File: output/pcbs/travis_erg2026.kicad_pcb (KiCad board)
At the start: 2 copper layers, 167.2 x 170.9 mm, 182 parts

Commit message: bunch of documentation
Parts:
- C10, C11, C12, C13, C14, C15, C16, C17, C18, C19, C2, C20, C21, C22, C23, C24, C25, C26, C27, C28, C29, C3, C30, C31, C32, C33, C34, C35, C36, C37, C38, C39, C4, C40, C41, C5, C6, C7, C8, C9: value C_1206_3216Metric -> C710467
- LED1, LED10, LED11, LED12, LED13, LED14, LED15, LED16, LED17, LED18, LED19, LED2, LED20, LED21, LED22, LED23, LED24, LED25, LED26, LED27, LED28, LED29, LED3, LED30, LED31, LED32, LED33, LED34, LED35, LED36, LED37, LED38, LED39, LED4, LED40, LED5, LED6, LED7, LED8, LED9: value SK6812mini-e -> C5378731
- S1, S10, S11, S12, S13, S14, S15, S16, S17, S18, S19, S2, S20, S21, S22, S23, S24, S25, S26, S27, S28, S29, S3, S30, S31, S32, S33, S34, S35, S36, S37, S38, S39, S4, S40, S5, S6, S7, S8, S9: value Kailh MX Switch Sockets -> C41430893

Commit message: BOM and CPL progress
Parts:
- LED1, LED10, LED11, LED12, LED13, LED14, LED15, LED16, LED17, LED18, LED19, LED2, LED20, LED21, LED22, LED23, LED24, LED25, LED26, LED27, LED28, LED29, LED3, LED30, LED31, LED32, LED33, LED34, LED35, LED36, LED37, LED38, LED39, LED4, LED40, LED5, LED6, LED7, LED8, LED9: footprint travis:led_SK6812mini-e (per-key, single-side) -> led_SK6812mini-e (per-key, single-side)
- S1, S10, S11, S12, S13, S14, S15, S16, S17, S18, S19, S2, S20, S21, S22, S23, S24, S25, S26, S27, S28, S29, S3, S30, S31, S32, S33, S34, S35, S36, S37, S38, S39, S4, S40, S5, S6, S7, S8, S9: footprint travis:MX -> MX

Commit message: attempt 2
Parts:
- removed LED1, LED2, LED3, LED4, LED5, LED6, LED7, LED8, LED9: C5378731, led_SK6812mini-e (per-key, single-side)
- added LED01: C5378731, led_SK6812mini-e (per-key, single-side), B.Cu at (176.2, 89.1)
- added LED02: C5378731, led_SK6812mini-e (per-key, single-side), B.Cu at (153.9, 87.1)
- added LED03: C5378731, led_SK6812mini-e (per-key, single-side), B.Cu at (132.0, 85.7)
- added LED04: C5378731, led_SK6812mini-e (per-key, single-side), B.Cu at (110.0, 84.7)
- added LED05: C5378731, led_SK6812mini-e (per-key, single-side), B.Cu at (88.0, 86.1)
- added LED06: C5378731, led_SK6812mini-e (per-key, single-side), B.Cu at (66.1, 87.8)
- added LED07: C5378731, led_SK6812mini-e (per-key, single-side), B.Cu at (43.9, 90.1)
- added LED08: C5378731, led_SK6812mini-e (per-key, single-side), B.Cu at (45.0, 111.2)
- added LED09: C5378731, led_SK6812mini-e (per-key, single-side), B.Cu at (66.9, 108.8)
- D1, D10, D11, D12, D13, D14, D15, D16, D17, D18, D19, D2, D20, D21, D22, D23, D24, D25, D26, D27, D28, D29, D3, D30, D31, D32, D33, D34, D35, D36, D37, D38, D39, D4, D40, D5, D6, D7, D8, D9: value D_1206_3216Metric -> C7420318
- MCU1: value RP2040 Pro Micro -> RP2040 Community Edition
- S1, S10, S11, S12, S13, S14, S15, S16, S17, S18, S19, S2, S20, S21, S22, S23, S24, S25, S26, S27, S28, S29, S3, S30, S31, S32, S33, S34, S35, S36, S37, S38, S39, S4, S40, S5, S6, S7, S8, S9: footprint MX -> ceoloide:switch_mx; moved to B.Cu
- moved LED21 137.1 mm to (46.1, 132.2), turned to 183 degrees
- moved LED35 107.2 mm to (48.3, 174.2), turned to 183 degrees
- moved LED20 106.4 mm to (67.6, 129.9), turned to 182 degrees
- moved LED29 106.4 mm to (171.8, 173.2), turned to 177 degrees
- moved LED37 104.5 mm to (89.9, 191.3), turned to 1 degrees
- moved LED36 102.2 mm to (59.7, 194.5), turned to 4 degrees
- moved LED19 94.4 mm to (88.8, 128.2), turned to 181 degrees
- moved LED40 84.7 mm to (160.4, 193.5), turned to -4 degrees
- moved LED28 83.8 mm to (172.9, 152.2), turned to -3 degrees
- moved LED26 75.5 mm to (130.9, 148.9), turned to -1 degrees
- moved LED27 74.2 mm to (151.7, 150.2), turned to -2 degrees
- moved LED34 66.0 mm to (69.1, 172.0), turned to 182 degrees
- moved LED13 65.8 mm to (153.2, 108.1), turned to -2 degrees
- moved LED10 65.4 mm to (88.4, 107.1), turned to 1 degrees
- moved LED32 63.2 mm to (110.0, 168.9), turned to 180 degrees
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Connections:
- LED10 pad 2: LED_33 -> LED11
- LED10 pad 4: LED_32 -> LED10
- LED11 pad 2: LED_19 -> LED12
- LED11 pad 4: LED_18 -> LED11
- LED12 pad 2: LED_5 -> LED13
- LED12 pad 4: LED_4 -> LED12
- LED13 pad 2: LED_32 -> LED14
- LED13 pad 4: LED_31 -> LED13
- LED14 pad 2: LED_18 -> LED15
- LED14 pad 4: LED_17 -> LED14
- LED15 pad 2: LED_4 -> LED16
- LED15 pad 4: LED_3 -> LED15
- LED16 pad 2: LED_31 -> LED17
- LED16 pad 4: LED_30 -> LED16
- LED17 pad 2: LED_17 -> LED18
- LED17 pad 4: LED_16 -> LED17
- LED18 pad 2: LED_3 -> LED19
- LED18 pad 4: LED_2 -> LED18
- LED19 pad 2: LED_30 -> LED20
- LED19 pad 4: LED_29 -> LED19
- LED20 pad 2: LED_16 -> LED21
- LED20 pad 4: LED_15 -> LED20
- LED21 pad 2: LED_2 -> LED22
- LED21 pad 4: LED_1 -> LED21
- LED22 pad 2: LED_37 -> LED23
- LED22 pad 4: LED_36 -> LED22
- LED23 pad 2: LED_23 -> LED24
- LED23 pad 4: LED_22 -> LED23
- LED24 pad 2: LED_9 -> LED25
- LED24 pad 4: LED_8 -> LED24
- LED25 pad 2: LED_24 -> LED26
- LED25 pad 4: LED_23 -> LED25
- LED26 pad 2: LED_10 -> LED27
- LED26 pad 4: LED_9 -> LED26
- LED27 pad 2: LED_38 -> LED28
- LED27 pad 4: LED_37 -> LED27
- LED28 pad 2: LED_25 -> LED29
- LED28 pad 4: LED_24 -> LED28
- LED29 pad 2: LED_11 -> LED30
- LED29 pad 4: LED_10 -> LED29
- LED30 pad 2: LED_39 -> LED31
- LED30 pad 4: LED_38 -> LED30
- LED31 pad 2: LED_26 -> LED32
- LED31 pad 4: LED_25 -> LED31
- LED32 pad 2: LED_12 -> LED33
- LED32 pad 4: LED_11 -> LED32
- LED33 pad 2: LED_40 -> LED34
- LED33 pad 4: LED_39 -> LED33
- LED34 pad 2: LED_27 -> LED35
- LED34 pad 4: LED_26 -> LED34
- LED35 pad 2: LED_13 -> LED36
- LED35 pad 4: LED_12 -> LED35
- LED36 pad 2: LED_28 -> LED37
- LED36 pad 4: LED_27 -> LED36
- LED37 pad 2: LED_14 -> LED38
- LED37 pad 4: LED_13 -> LED37
- LED38 pad 2: (no net) -> LED39
- LED38 pad 4: LED_40 -> LED38
- LED39 pad 2: LED_29 -> LED40
- LED39 pad 4: LED_28 -> LED39
- LED40 pad 2: LED_15 -> (no net)
- LED40 pad 4: LED_14 -> LED40
- MCU1 pad 31: LED_1 -> LED01
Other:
- board text added: "LED01"
- board text added: "LED02"
- board text added: "LED03"
- board text added: "LED04"
- board text added: "LED05"
- board text added: "LED06"
- board text added: "LED07"
- board text added: "LED08"
- board text added: "LED09"
- board text added: "LED10"
- board text added: "LED11"
- board text added: "LED12"
- board text added: "LED13"
- board text added: "LED14"
- board text added: "LED15"
- board text added: "LED16"
- board text added: "LED17"
- board text added: "LED18"
- board text added: "LED19"
- board text added: "LED20"
- board text added: "LED21"
- board text added: "LED22"
- board text added: "LED23"
- board text added: "LED24"
- board text added: "LED25"
- board text added: "LED26"
- board text added: "LED27"
- board text added: "LED28"
- board text added: "LED29"
- board text added: "LED30"
- board text added: "LED31"
- board text added: "LED32"
- board text added: "LED33"
- board text added: "LED34"
- board text added: "LED35"
- board text added: "LED36"
- board text added: "LED37"
- board text added: "LED38"
- board text added: "LED39"
- board text added: "LED40"
- board text removed: "LED_1"
- board text removed: "LED_10"
- board text removed: "LED_11"
- board text removed: "LED_12"
- board text removed: "LED_13"
- board text removed: "LED_14"
- board text removed: "LED_15"
- board text removed: "LED_16"
- board text removed: "LED_17"
- board text removed: "LED_18"
- board text removed: "LED_19"
- board text removed: "LED_2"
- board text removed: "LED_20"
- board text removed: "LED_21"
- board text removed: "LED_22"
- board text removed: "LED_23"
- board text removed: "LED_24"
- board text removed: "LED_25"
- board text removed: "LED_26"
- board text removed: "LED_27"
- board text removed: "LED_28"
- board text removed: "LED_29"
- board text removed: "LED_3"
- board text removed: "LED_30"
- board text removed: "LED_31"
- board text removed: "LED_32"
- board text removed: "LED_33"
- board text removed: "LED_34"
- board text removed: "LED_35"
- board text removed: "LED_36"
- board text removed: "LED_37"
- board text removed: "LED_38"
- board text removed: "LED_39"
- board text removed: "LED_4"
- board text removed: "LED_40"
- board text removed: "LED_5"
- board text removed: "LED_6"
- board text removed: "LED_7"
- board text removed: "LED_8"
- board text removed: "LED_9"
- board text removed: "S1"
- board text removed: "S10"
- board text removed: "S11"
- board text removed: "S12"
- board text removed: "S13"
- board text removed: "S14"
- board text removed: "S15"
- board text removed: "S16"
- board text removed: "S17"
- board text removed: "S18"
- board text removed: "S19"
- board text removed: "S2"
- board text removed: "S20"
- board text removed: "S21"
- board text removed: "S22"
- board text removed: "S23"
- board text removed: "S24"
- board text removed: "S25"
- board text removed: "S26"
- board text removed: "S27"
- board text removed: "S28"
- board text removed: "S29"
- board text removed: "S3"
- board text removed: "S30"
- board text removed: "S31"
- board text removed: "S32"
- board text removed: "S33"
- board text removed: "S34"
- board text removed: "S35"
- board text removed: "S36"
- board text removed: "S37"
- board text removed: "S38"
- board text removed: "S39"
- board text removed: "S4"
- board text removed: "S40"
- board text removed: "S5"
- board text removed: "S6"
- board text removed: "S7"
- board text removed: "S8"
- board text removed: "S9"

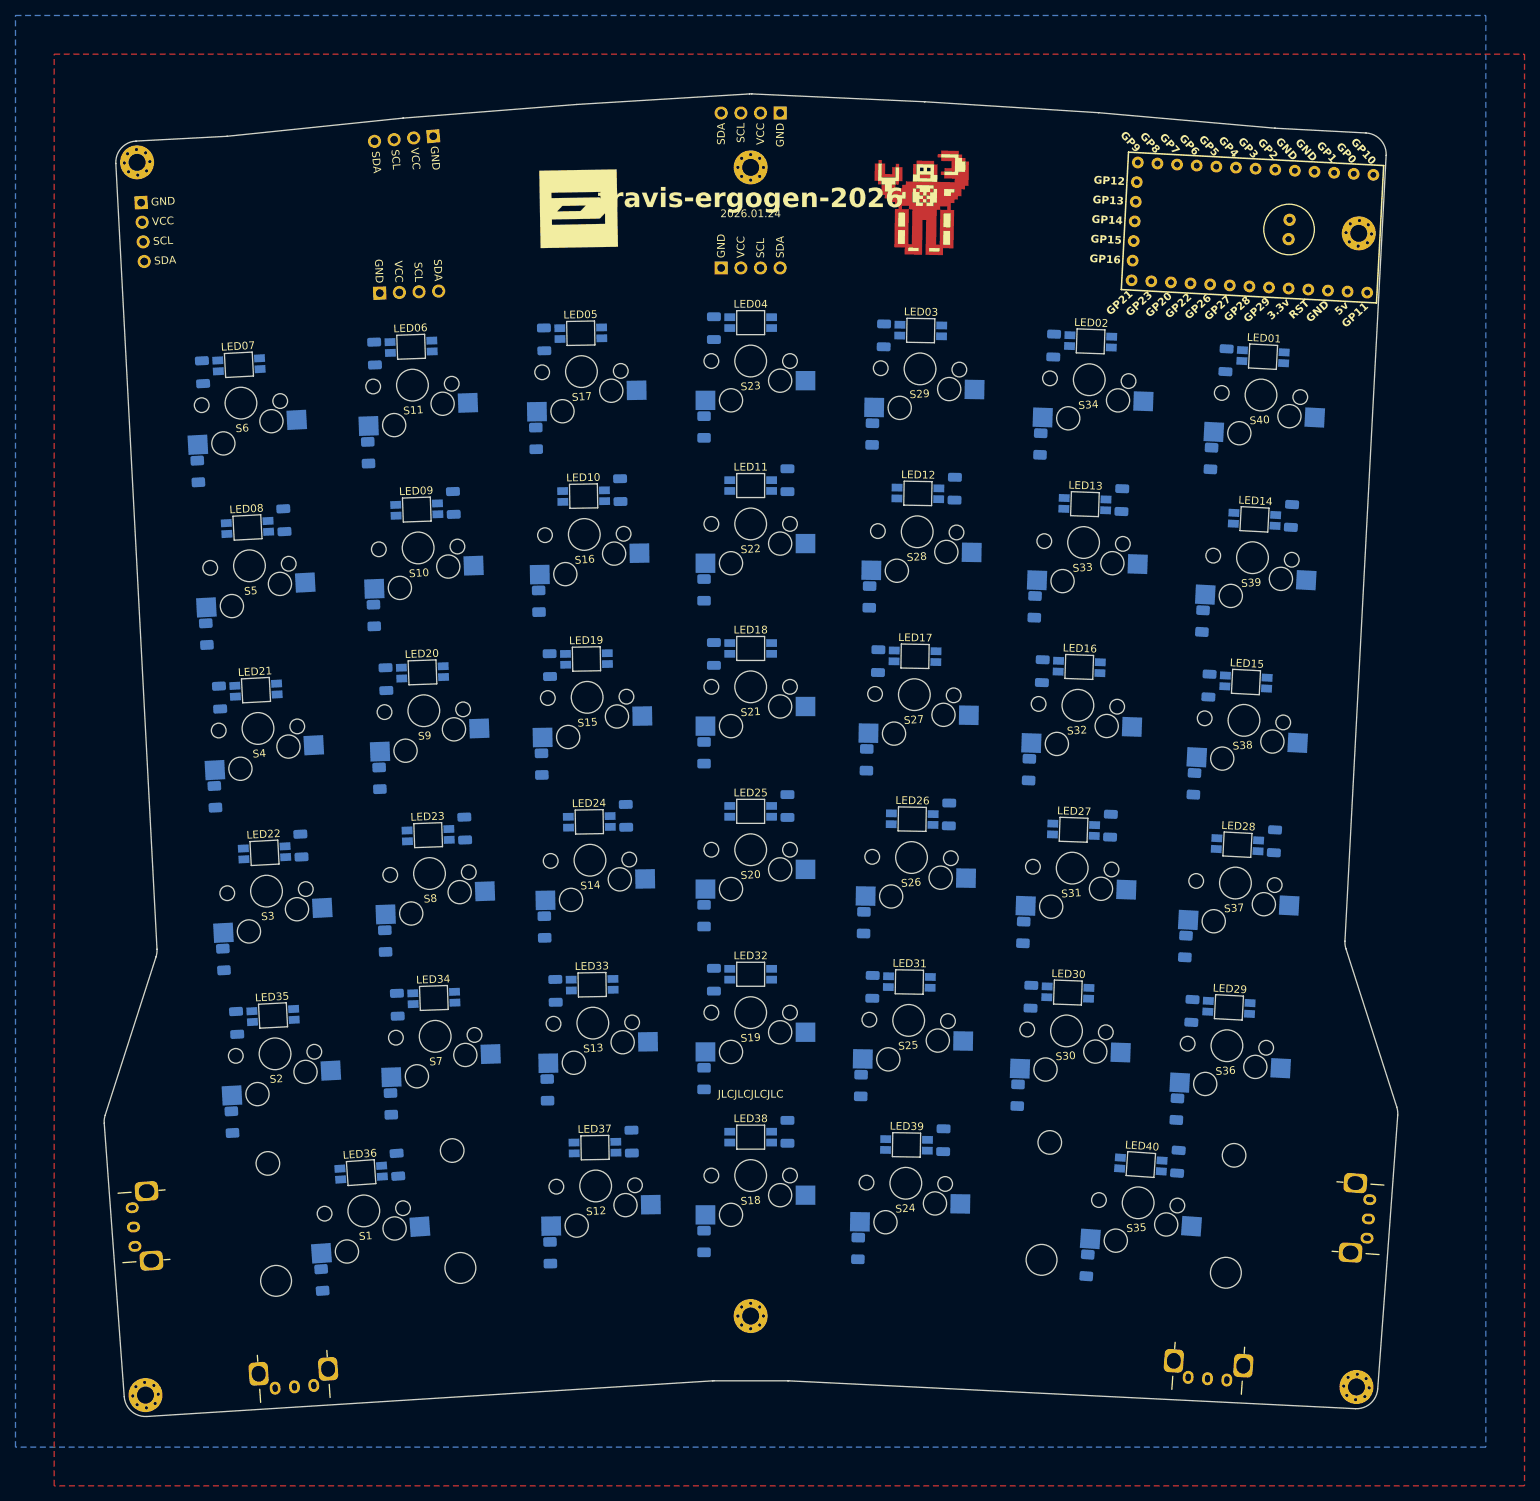
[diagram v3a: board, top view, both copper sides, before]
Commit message: fix encorder, organize datasheets, add easy routes and vias
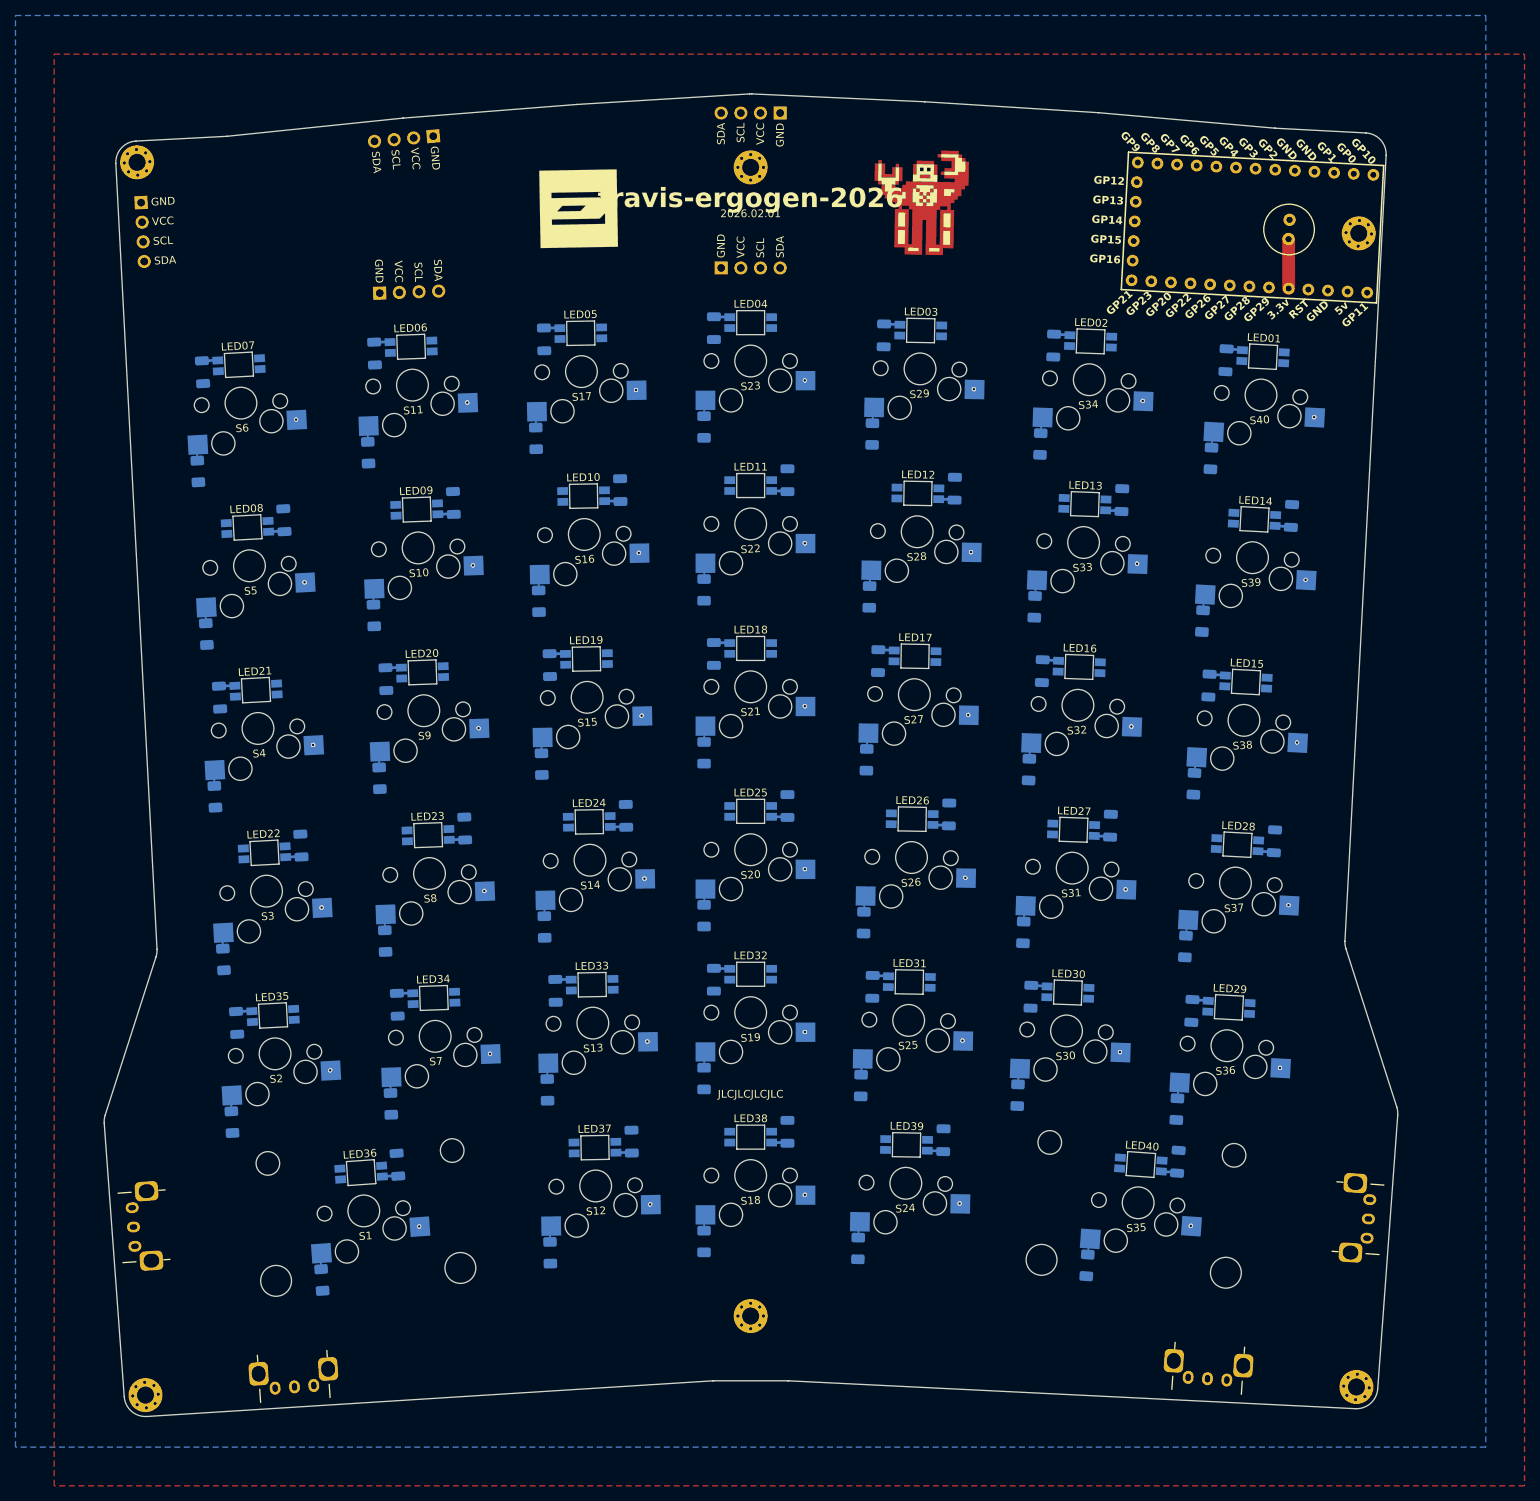
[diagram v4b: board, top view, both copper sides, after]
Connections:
- MCU1 pad 8: encC -> encB
- ROT1 pad B: GND -> encB
- ROT1 pad C: encC -> GND
- ROT2 pad B: GND -> encB
- ROT2 pad C: encC -> GND
- ROT3 pad B: GND -> encB
- ROT3 pad C: encC -> GND
- ROT4 pad B: GND -> encB
- ROT4 pad C: encC -> GND
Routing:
- net VCC: track 0.00 -> 78.8 mm
- net row3: track 0.00 -> 15.1 mm
- net row1: track 0.00 -> 15.1 mm
- net row4: track 0.00 -> 15.1 mm
- net row5: track 0.00 -> 15.1 mm
- net row2: track 0.00 -> 15.1 mm
- net row0: track 0.00 -> 10.8 mm
- net col6: vias 0 -> 6
- net col5: vias 0 -> 5
- net col4: vias 0 -> 6
- net col3: vias 0 -> 6
- net col2: vias 0 -> 6
- net col1: vias 0 -> 5
- net col0: vias 0 -> 6
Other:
- board text added: "2026.02.01"
- board text removed: "2026.01.24"

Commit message: v3 routed
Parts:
- added R1: 510k, Resistor_THT:R_Axial_DIN0207_L6.3mm_D2.5mm_P10.16mm_Horizontal, B.Cu at (169.3, 76.8)
- added R2: 510k, Resistor_THT:R_Axial_DIN0207_L6.3mm_D2.5mm_P10.16mm_Horizontal, B.Cu at (172.3, 77.0)
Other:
- board text added: "2026.02.02"
- board text removed: "2026.02.01"
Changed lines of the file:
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@@
   (title_block
     (title "travis_erg2026")
-    (date "2026-02-01")
-    (rev "2026.02.01")
+    (date "2026-02-02")
+    (rev "2026.02.02")
     (company "Travis Hardiman")
   )
@@
   )
 )
+    (module "Resistor_THT:R_Axial_DIN0207_L6.3mm_D2.5mm_P10.16mm_Horizontal" (layer B.Cu)
+    (descr "Resistor, Axial_DIN0207 series, Axial, Horizontal, pin pitch=10.16mm, 0.25W = 1/4W, length*diameter=6.3*2.5mm^2, http://cdn-reichelt.de/documents/datenblatt/B400/1_4W%23YAG.pdf")
+    (tags "Resistor Axial_DIN0207 series Axial Horizontal pin pitch 10.16mm 0.25W = 1/4W length 6.3mm diameter 2.5mm")
+    (at 169.34146640000006 76.82391790000003 87)
+    (fp_text reference "R1" (at 5.08 -2.37) (layer B.SilkS) hide
+      (effects (font (size 1 1) (thickness 0.15)))
+    )
+    (fp_text value "510k" (at 5.08 2.37) (layer B.Fab) hide
+      (effects (font (size 1 1) (thickness 0.15)))
+    )
+    (fp_line (start 1.93 -1.25) (end 1.93 1.25) (layer B.Fab) (width 0.1))
+    (fp_line (start 1.93 1.25) (end 8.23 1.25) (layer B.Fab) (width 0.1))
+    (fp_line (start 8.23 1.25) (end 8.23 -1.25) (layer B.Fab) (width 0.1))
+    (fp_line (start 8.23 -1.25) (end 1.93 -1.25) (layer B.Fab) (width 0.1))
+    (fp_line (start 0 0) (end 1.93 0) (layer B.Fab) (width 0.1))
+    (fp_line (start 10.16 0) (end 8.23 0) (layer B.Fab) (width 0.1))
+    (fp_line (start 1.81 -1.37) (end 1.81 1.37) (layer B.SilkS) (width 0.12))
+    (fp_line (start 1.81 1.37) (end 8.35 1.37) (layer B.SilkS) (width 0.12))
+    (fp_line (start 8.35 1.37) (end 8.35 -1.37) (layer B.SilkS) (width 0.12))
+    (fp_line (start 8.35 -1.37) (end 1.81 -1.37) (layer B.SilkS) (width 0.12))
+    (fp_line (start 1.04 0) (end 1.81 0) (layer B.SilkS) (width 0.12))
+    (fp_line (start 9.12 0) (end 8.35 0) (layer B.SilkS) (width 0.12))
+    (fp_line (start -1.05 -1.5) (end -1.05 1.5) (layer B.CrtYd) (width 0.05))
+    (fp_line (start -1.05 1.5) (end 11.21 1.5) (layer B.CrtYd) (width 0.05))
+    (fp_line (start 11.21 1.5) (end 11.21 -1.5) (layer B.CrtYd) (width 0.05))
+    (fp_line (start 11.21 -1.5) (end -1.05 -1.5) (layer B.CrtYd) (width 0.05))
+    (pad 1 thru_hole circle (at 0 0) (size 1.6 1.6) (drill 0.8) (layers *.Cu *.Mask) (net 26 "VCC"))
+    (pad 2 thru_hole oval (at 10.16 0 87) (size 1.6 1.6) (drill 0.8) (layers *.Cu *.Mask) (net 8 "encA"))
+    (fp_text user %R (at 5.08 0) (layer B.Fab)
+      (effects (font (size 1 1) (thickness 0.15)))
+    )
+    (model ${KISYS3DMOD}/Resistor_THT.3dshapes/R_Axial_DIN0207_L6.3mm_D2.5mm_P10.16mm_Horizontal.wrl
+      (at (xyz 0 0 0))
+      (scale (xyz 1 1 1))
+      (rotate (xyz 0 0 0))
+    )
+  )
+    (module "Resistor_THT:R_Axial_DIN0207_L6.3mm_D2.5mm_P10.16mm_Horizontal" (layer B.Cu)
+    (descr "Resistor, Axial_DIN0207 series, Axial, Horizontal, pin pitch=10.16mm, 0.25W = 1/4W, length*diameter=6.3*2.5mm^2, http://cdn-reichelt.de/documents/datenblatt/B400/1_4W%23YAG.pdf")
+    (tags "Resistor Axial_DIN0207 series Axial Horizontal pin pitch 10.16mm 0.25W = 1/4W length 6.3mm diameter 2.5mm")
+    (at 172.33735500000006 76.98092570000003 87)
+    (fp_text reference "R2" (at 5.08 -2.37) (layer B.SilkS) hide
+      (effects (font (size 1 1) (thickness 0.15)))
+    )
+    (fp_text value "510k" (at 5.08 2.37) (layer B.Fab) hide
+      (effects (font (size 1 1) (thickness 0.15)))
+    )
+    (fp_line (start 1.93 -1.25) (end 1.93 1.25) (layer B.Fab) (width 0.1))
+    (fp_line (start 1.93 1.25) (end 8.23 1.25) (layer B.Fab) (width 0.1))
+    (fp_line (start 8.23 1.25) (end 8.23 -1.25) (layer B.Fab) (width 0.1))
+    (fp_line (start 8.23 -1.25) (end 1.93 -1.25) (layer B.Fab) (width 0.1))
+    (fp_line (start 0 0) (end 1.93 0) (layer B.Fab) (width 0.1))
+    (fp_line (start 10.16 0) (end 8.23 0) (layer B.Fab) (width 0.1))
+    (fp_line (start 1.81 -1.37) (end 1.81 1.37) (layer B.SilkS) (width 0.12))
+    (fp_line (start 1.81 1.37) (end 8.35 1.37) (layer B.SilkS) (width 0.12))
+    (fp_line (start 8.35 1.37) (end 8.35 -1.37) (layer B.SilkS) (width 0.12))
+    (fp_line (start 8.35 -1.37) (end 1.81 -1.37) (layer B.SilkS) (width 0.12))
+    (fp_line (start 1.04 0) (end 1.81 0) (layer B.SilkS) (width 0.12))
+    (fp_line (start 9.12 0) (end 8.35 0) (layer B.SilkS) (width 0.12))
+    (fp_line (start -1.05 -1.5) (end -1.05 1.5) (layer B.CrtYd) (width 0.05))
+    (fp_line (start -1.05 1.5) (end 11.21 1.5) (layer B.CrtYd) (width 0.05))
+    (fp_line (start 11.21 1.5) (end 11.21 -1.5) (layer B.CrtYd) (width 0.05))
+    (fp_line (start 11.21 -1.5) (end -1.05 -1.5) (layer B.CrtYd) (width 0.05))
+    (pad 1 thru_hole circle (at 0 0) (size 1.6 1.6) (drill 0.8) (layers *.Cu *.Mask) (net 26 "VCC"))
+    (pad 2 thru_hole oval (at 10.16 0 87) (size 1.6 1.6) (drill 0.8) (layers *.Cu *.Mask) (net 7 "encB"))
+    (fp_text user %R (at 5.08 0) (layer B.Fab)
+      (effects (font (size 1 1) (thickness 0.15)))
+    )
+    (model ${KISYS3DMOD}/Resistor_THT.3dshapes/R_Axial_DIN0207_L6.3mm_D2.5mm_P10.16mm_Horizontal.wrl
+      (at (xyz 0 0 0))
+      (scale (xyz 1 1 1))
+      (rotate (xyz 0 0 0))
+    )
+  )
 (footprint "Alps-EC10E1220501"
 	(version 20241229)
@@
     )
   )
-  (gr_text "2026.02.01"
+  (gr_text "2026.02.02"
     (at 110.0025666 70.60314029999996 0)
     (layer "F.SilkS" )
